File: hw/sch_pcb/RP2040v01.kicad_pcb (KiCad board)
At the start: 2 copper layers, 50.3 x 50.3 mm, 46 parts, among them J1 HEADER_1x03, J2 USBC_USB4105-GF-A, J3 HEADER_1x03, J4 HEADER_1x10, J5 HEADER_1x10, J6 HEADER_1x10, J7 HEADER_1x10, J8 HEADER_2x05, Q1 BC817-25, SW1 434133025816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

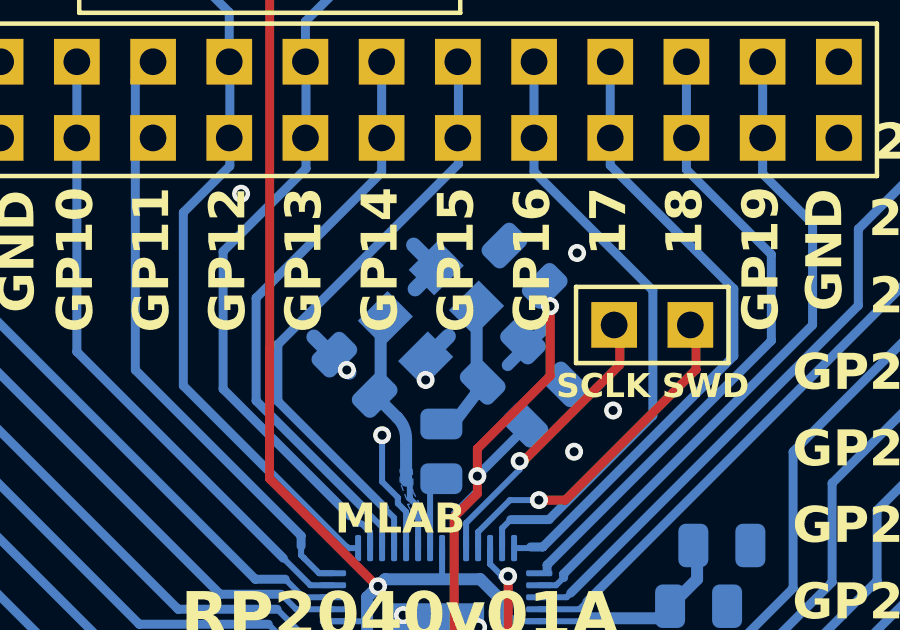
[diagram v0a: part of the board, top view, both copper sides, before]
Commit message: Update project to KiCADv9.
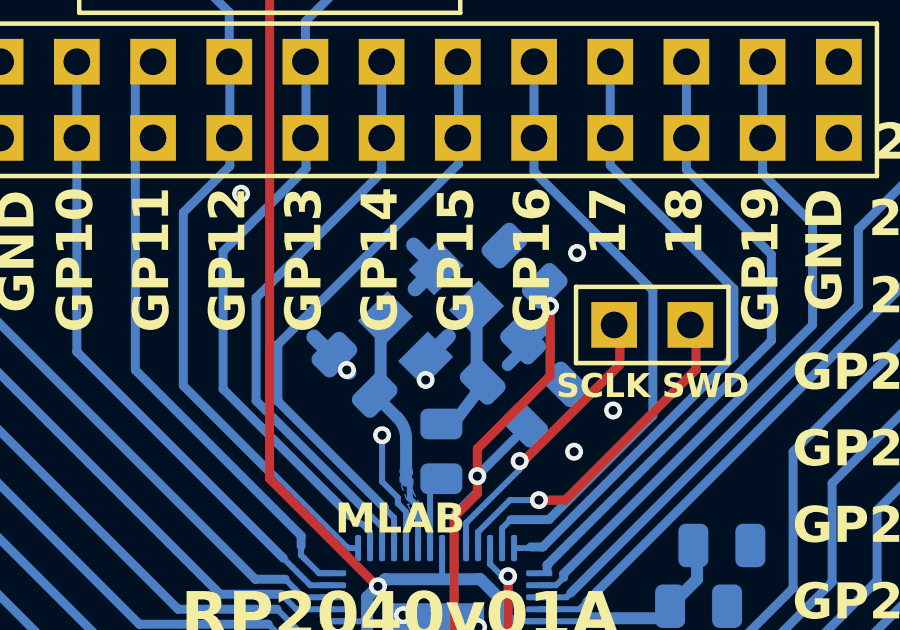
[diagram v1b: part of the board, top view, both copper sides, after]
